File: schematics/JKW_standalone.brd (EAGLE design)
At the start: 159.4 x 80.7 mm, 226 parts, among them IC1 4093D, IC2 AT-MEGA-8L, IC4 ATMEGA2560-16AU, Q1 BSS84, Q10 BSS84, Q11 BSS84, Q2 BSS84, Q3 BSS84, Q4 BSS84, Q5 BSS84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

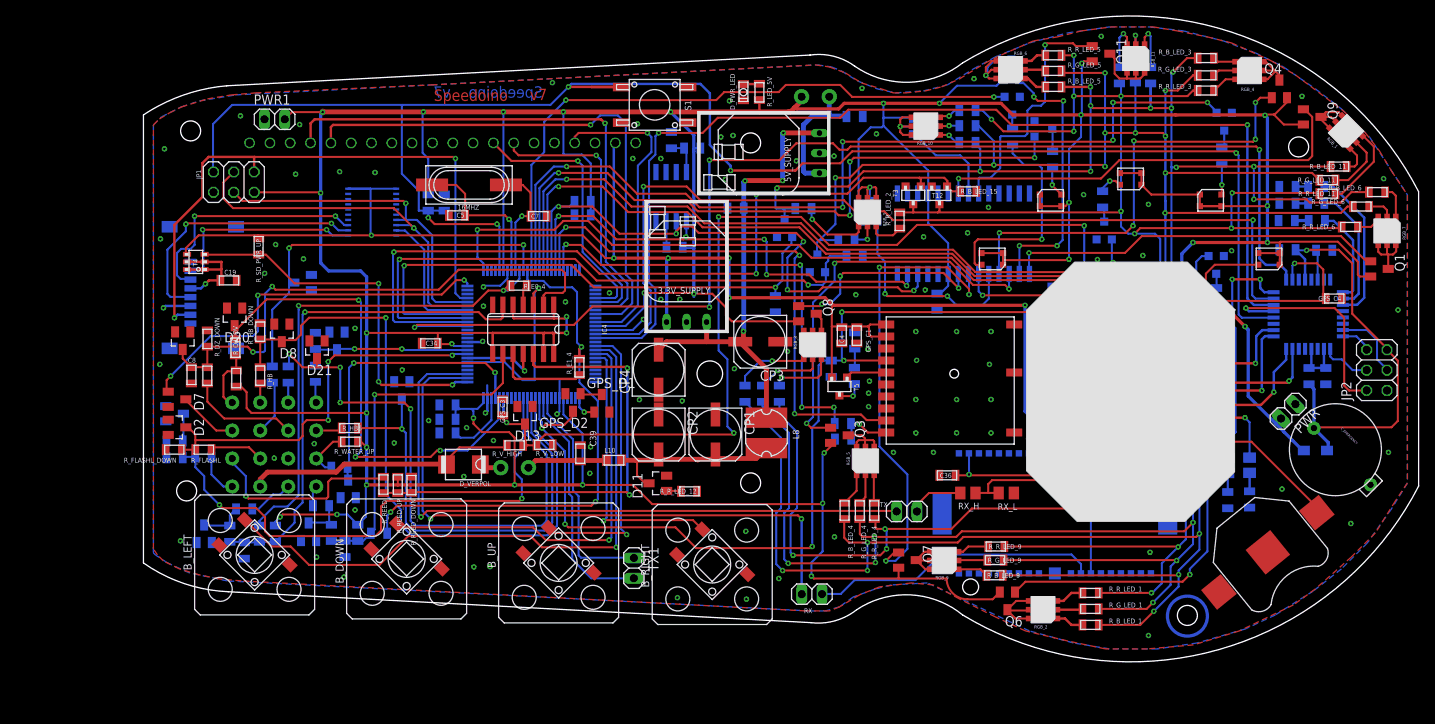
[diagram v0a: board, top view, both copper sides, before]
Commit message: Added correct overvoltage z-diode
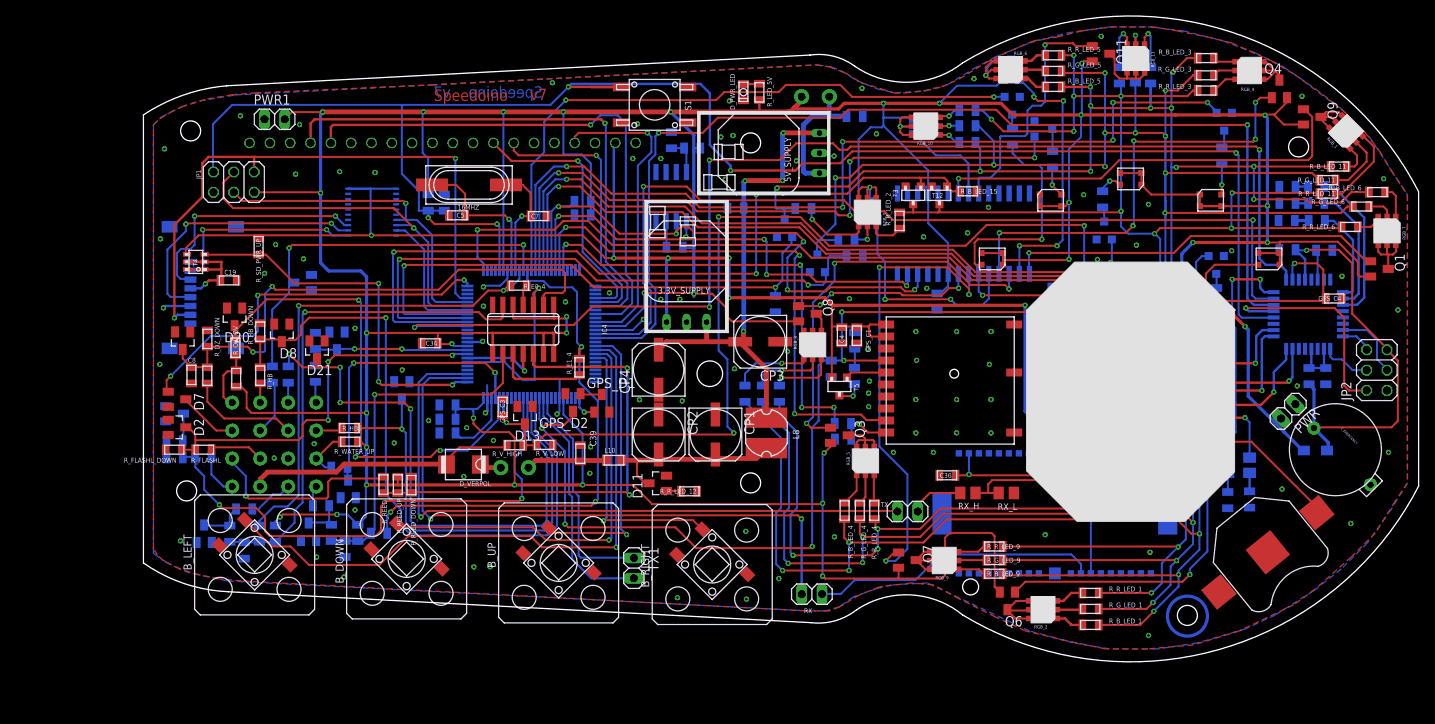
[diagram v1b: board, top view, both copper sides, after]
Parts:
- removed R_B_LED_0, R_G_LED_0: 24R, RCLDT:0805
- removed U$1: CLP6B-WKW-CD0E0233, Kolja:PLCC-6
- added U$22: CLM4B-RKW-CWAXBAA3, Kolja:PLCC-4
- R_R_LED_0: value 24R -> 52R
- moved R_B_LED_9 0.20 mm to (106.4, 6.40)
- moved R_R_LED_9 0.20 mm to (106.4, 9.80)
- moved R_G_LED_9 0.10 mm to (106.4, 8.10)
- moved TX 0.10 mm to (95.5, 14.2)
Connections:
- removed net N$63: R_G_LED_0.1, U$1.2-
- removed net N$65: R_B_LED_0.1, U$1.3-
- net N$16: now also U$22.P$4; no longer U$1.1-
- net N$71: no longer R_B_LED_0.2, R_G_LED_0.2
- net VDD: now also U$22.P$1, U$22.P$2, U$22.P$3; no longer U$1.1+, U$1.2+, U$1.3+
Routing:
- net N$16: track 4.39 -> 9.82 mm
- net N$65: track 4.53 -> 0.00 mm, vias 1 -> 0
- net N$63: track 4.26 -> 0.00 mm, vias 1 -> 0
- net N$71: track 6.97 -> 2.72 mm
- net RED_INSTR: track 287.1 -> 283.6 mm
- net VDD: track 752.7 -> 756.0 mm
- net N$105: track 25.7 -> 23.0 mm
- net BLUE_INSTR: track 309.2 -> 308.4 mm
- net N$81: track 8.58 -> 9.34 mm
- net N$82: track 9.62 -> 10.3 mm
- net GREEN_INSTR: track 311.7 -> 311.1 mm
- net GND: vias 99 -> 102

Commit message: added reset from ATM328 to 2560
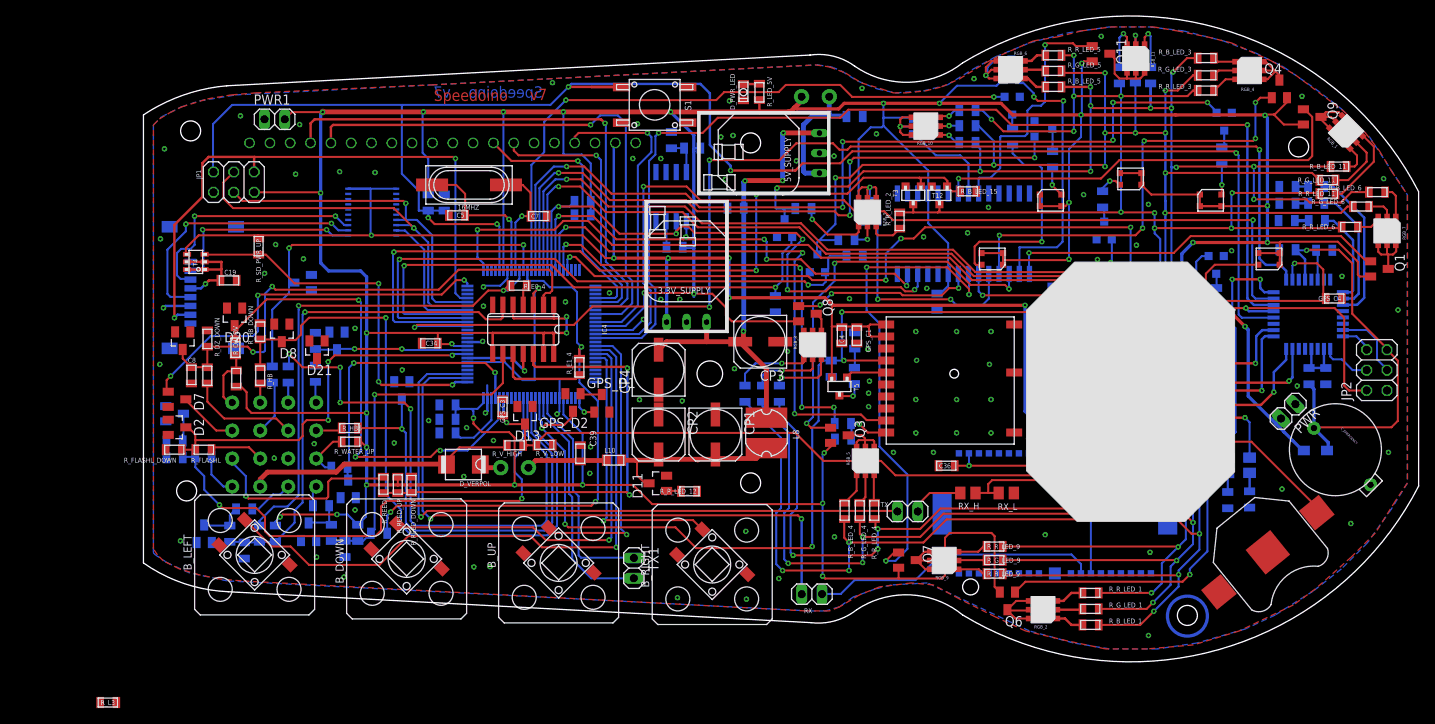
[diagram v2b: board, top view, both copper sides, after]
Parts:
- added R_L3: 1k, RCLDT:0805
- IC2: value AT-MEGA-8L -> AT-MEGA-328P-AU
- moved C36 1.20 mm to (100.4, 19.9)
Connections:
- net RESETAVR_AT8: now also IC4.47, R_L3.2
- net VDD: now also R_L3.1
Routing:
- net RESETAVR_AT8: track 28.0 -> 130.2 mm, vias 1 -> 6
- net A2: track 164.4 -> 148.7 mm, vias 6 -> 4
- net DZ: track 67.5 -> 64.3 mm
- net +3V3_EXT: track 220.7 -> 218.1 mm
- net N$104: track 57.7 -> 59.9 mm
- net SDA: track 62.4 -> 61.3 mm
- net RX1: track 68.4 -> 69.0 mm
- net D7: track 103.0 -> 102.5 mm
- net N$102: track 27.0 -> 27.5 mm
- net RED_INSTR: track 283.6 -> 283.8 mm, vias 15 -> 16
- net N$99: vias 4 -> 2

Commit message: Moved LED's to port expander
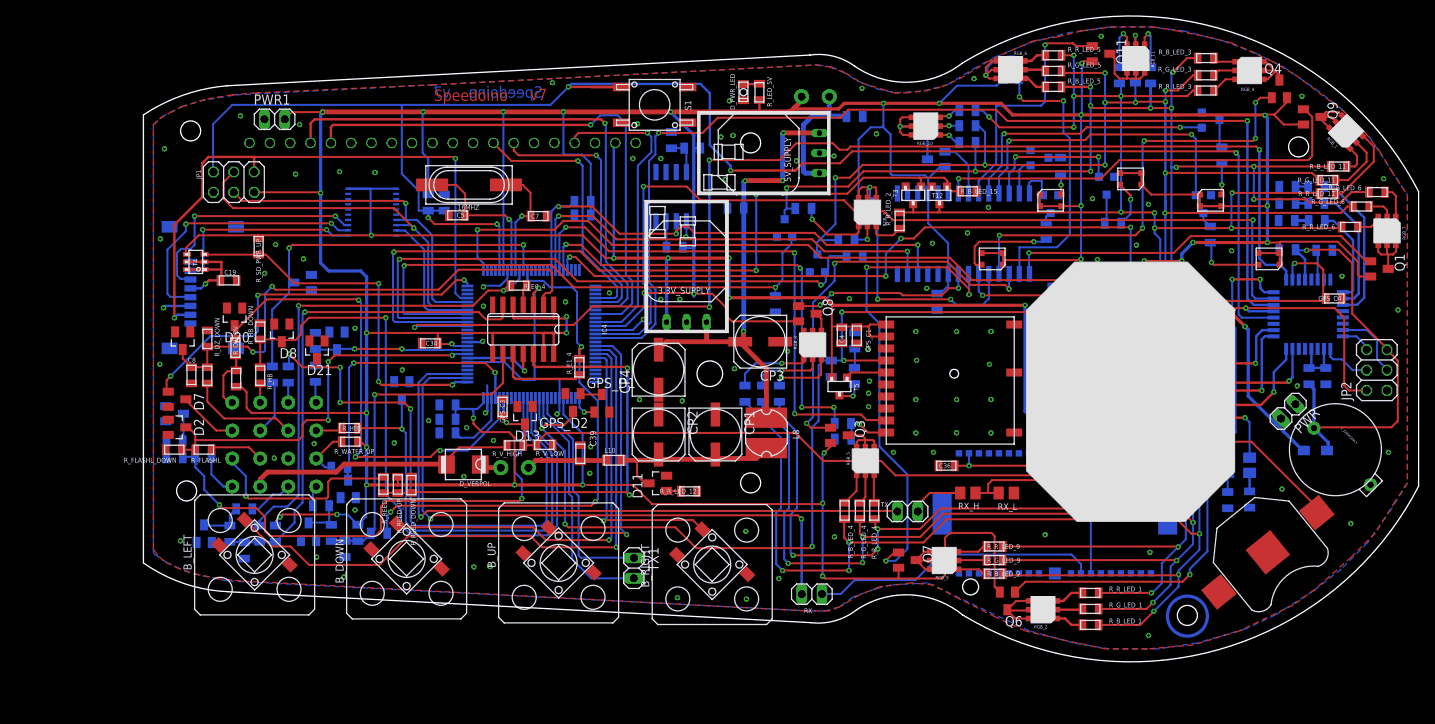
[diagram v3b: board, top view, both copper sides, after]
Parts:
- moved R_L3 139.8 mm to (125.0, 43.1), flipped to the bottom, turned to 270 degrees
- moved T8 13.2 mm to (113.4, 52.6)
- moved R_OIL 12.5 mm to (112.8, 49.2)
- moved T7 7.77 mm to (132.5, 52.6)
- moved R_HIGHB 7.74 mm to (133.3, 48.8)
- moved T6 5.61 mm to (120.4, 54.9), turned to 0 degrees
- moved Q10 4.40 mm to (99.1, 58.2), turned to 270 degrees
- moved T10 3.63 mm to (112.0, 58.4)
- moved R_N 3.27 mm to (121.2, 50.2), turned to 0 degrees
- moved T9 1.71 mm to (133.4, 63.1), turned to 270 degrees
- moved R_BL_L 1.28 mm to (114.7, 57.4)
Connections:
- new net PE_A3: T9.1, U$19.24
- new net PE_A4: T7.1, U$19.25
- new net PE_A5: T6.1, U$19.26
- new net PE_A6: T10.1, U$19.27
- new net PE_A7: T8.1, U$19.28
- net D42: no longer T7.1
- net D43: no longer T6.1
- net D44: no longer T10.1
- net D45: no longer T9.1
- net D46: no longer T8.1
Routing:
- net D45: track 112.6 -> 0.00 mm, vias 6 -> 0
- net D42: track 99.1 -> 0.00 mm, vias 2 -> 0
- net D43: track 89.6 -> 0.00 mm, vias 2 -> 0
- net D44: track 84.7 -> 0.00 mm, vias 4 -> 0
- net D46: track 79.3 -> 0.00 mm, vias 2 -> 0
- net PE_A4: track 0.00 -> 38.0 mm, vias 0 -> 2
- net PE_A3: track 0.00 -> 33.4 mm, vias 0 -> 2
- net PE_A5: track 0.00 -> 17.8 mm, vias 0 -> 2
- net N$25: track 26.4 -> 12.4 mm
- net VDD: track 756.0 -> 765.4 mm, vias 36 -> 38
- net SCL: track 71.1 -> 63.7 mm, vias 5 -> 3
- net PE_A7: track 0.00 -> 4.87 mm
- net N$107: track 12.0 -> 7.17 mm
- net PE_A6: track 0.00 -> 4.59 mm
- net GREEN_INSTR: track 310.9 -> 306.4 mm
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
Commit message: changed controller
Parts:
- removed IC2: AT-MEGA-328P-AU, µP´s+Pic´s:TQFP-32_7X7
- added U$1: ATMEGA328P-AU, Kolja:TQFP8
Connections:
- net A2: now also U$1.2; no longer IC2.2
- net ARD_RES_OUT: now also U$1.28; no longer IC2.28
- net CONNECT: now also U$1.32; no longer IC2.32
- net D6: now also U$1.1; no longer IC2.1
- net GND: now also U$1.21, U$1.3, U$1.5; no longer IC2.21, IC2.3, IC2.5
- net M1: now also U$1.23; no longer IC2.23
- net M2: now also U$1.24; no longer IC2.24
- net M3: now also U$1.25; no longer IC2.25
- net M4: now also U$1.26; no longer IC2.26
- net MISO_AT8: now also U$1.16; no longer IC2.16
- net MOSI_AT8: now also U$1.15; no longer IC2.15
- net N$14: now also U$1.11; no longer IC2.11
- net N$18: now also U$1.10; no longer IC2.10
- net N$20: now also U$1.9; no longer IC2.9
- net N$3: now also U$1.18, U$1.20; no longer IC2.18, IC2.20
- net RESETAVR_AT8: no longer IC2.29
- net RX3: now also U$1.31; no longer IC2.31
- net SCK_AT8: now also U$1.17; no longer IC2.17
- net TX3: now also U$1.30; no longer IC2.30
- net V_AT8_BUFFERED: now also U$1.4, U$1.6; no longer IC2.4, IC2.6
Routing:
- net V_AT8_BUFFERED: track 59.8 -> 53.7 mm
- net N$3: track 7.08 -> 2.93 mm
- net M1: track 17.0 -> 13.5 mm
- net RESETAVR_AT8: track 131.1 -> 128.0 mm
- net MOSI_AT8: track 9.06 -> 6.05 mm
- net TX3: track 134.1 -> 131.7 mm
- net RX3: track 115.1 -> 112.8 mm
- net N$14: track 19.6 -> 17.9 mm
- net A2: track 148.7 -> 147.0 mm
- net MISO_AT8: track 3.91 -> 2.21 mm
- net M4: track 29.6 -> 28.1 mm
- net N$18: track 16.1 -> 14.7 mm
- net M2: track 14.8 -> 13.5 mm
- net CONNECT: track 48.8 -> 47.6 mm
- net D6: track 152.0 -> 150.9 mm
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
